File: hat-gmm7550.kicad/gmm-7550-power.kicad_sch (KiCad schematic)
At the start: 47 parts, among them J5 DNI, J6 10144517-064802LF, J8 JTAG, Q1 NX6008NBK, Q2 NX6008NBK, Q3 NX6008NBK, Q4 FDC855N, U2 74LVC1G07, U3 ADM1177, U8 LSF0204PW, U9 LSF0204PW

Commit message: Change U2 footprint due to the part availability, revision and date are updated (HAT GMM-7550)
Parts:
- U2: footprint Package_TO_SOT_SMD:SOT-353_SC-70-5 -> Package_TO_SOT_SMD:SOT-23-5
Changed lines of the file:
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@@
   (title_block
     (title "40-pin GPIO HAT adapter for GMM-7550")
-    (date "2022-03-09")
-    (rev "1.0")
+    (date "2022-04-24")
+    (rev "1.1")
   )
   (junction (at 78.74 172.72) (diameter 0) (color 0 0 0 0)
@@
     (property "Reference" "U2" (id 0) (at 96.52 55.88 0))
     (property "Value" "74LVC1G07" (id 1) (at 100.33 62.23 0))
-    (property "Footprint" "Package_TO_SOT_SMD:SOT-353_SC-70-5" (id 2) (at 93.98 59.69 0)
-      (effects (font (size 1.27 1.27)) hide)
-    )
+    (property "Footprint" "Package_TO_SOT_SMD:SOT-23-5" (id 2) (at 93.98 59.69 0)
+      (effects (font (size 1.27 1.27)) hide)
+    )

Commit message: Update copyright years and increment revision
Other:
- note added: "Copyright (c) 2022-2024 Anton Kuzmin Licensed under CERN-OHL-P v2 https://github.com/gmm-7550/"
- note removed: "Copyright (c) 2022 Anton Kuzmin Licensed under CERN-OHL-P v2 https://github.com/ak-fau/gmm7550.git"
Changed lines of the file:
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@@
   (title_block
     (title "40-pin GPIO HAT adapter for GMM-7550")
-    (date "2022-04-24")
-    (rev "1.1")
+    (date "2024-01-27")
+    (rev "1.2")
   )
   (junction (at 78.74 172.72) (diameter 0) (color 0 0 0 0)
@@
     (effects (font (size 1.27 1.27)) (justify right bottom))
   )
-  (text "Copyright (c) 2022  Anton Kuzmin\nLicensed under CERN-OHL-P v2\nhttps://github.com/ak-fau/gmm7550.git"
+  (text "Copyright (c) 2022-2024  Anton Kuzmin\nLicensed under CERN-OHL-P v2\nhttps://github.com/gmm-7550/"
     (at 198.12 179.07 0)
     (effects (font (size 2.54 2.54)) (justify left bottom))

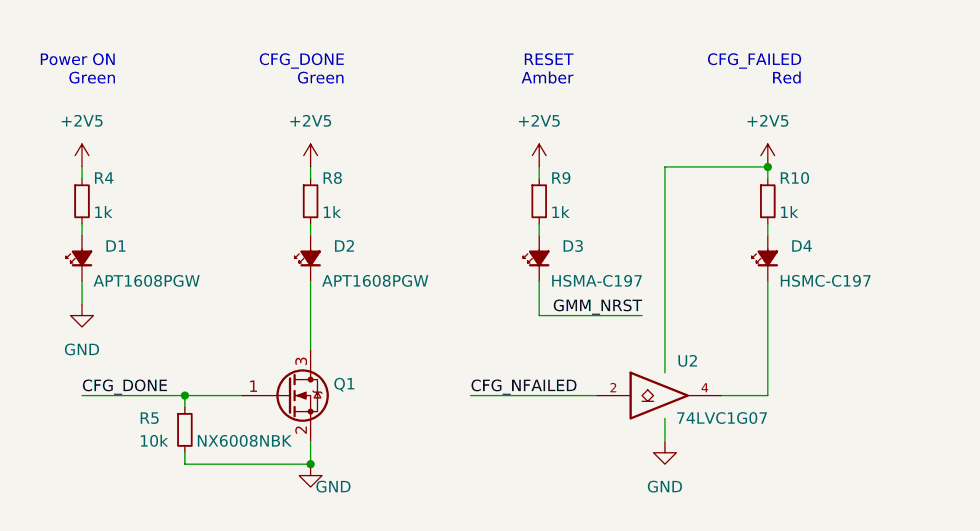
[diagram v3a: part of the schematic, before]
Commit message: Minor updates based on the test results
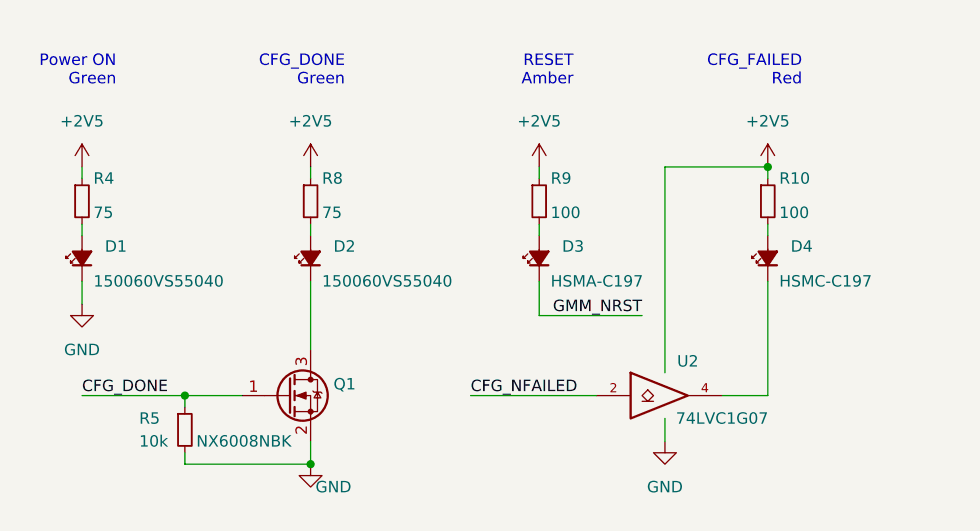
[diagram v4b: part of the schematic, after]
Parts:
- D1, D2: value APT1608PGW -> 150060VS55040
- R10, R9: value 1k -> 100
- R4, R8: value 1k -> 75
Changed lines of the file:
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@@
       (effects (font (size 1.27 1.27)) (justify left))
     )
-    (property "Value" "1k" (at 30.48 39.37 0)
+    (property "Value" "75" (at 30.48 39.37 0)
       (effects (font (size 1.27 1.27)) (justify left))
     )
@@
       (effects (font (size 1.27 1.27)) (justify right))
     )
-    (property "Value" "APT1608PGW" (at 55.88 46.99 90)
+    (property "Value" "150060VS55040" (at 55.88 46.99 90)
       (effects (font (size 1.27 1.27)) (justify right))
     )
@@
       (effects (font (size 1.27 1.27)) (justify left))
     )
-    (property "Value" "1k" (at 81.28 39.37 0)
+    (property "Value" "100" (at 81.28 39.37 0)
       (effects (font (size 1.27 1.27)) (justify left))
     )
@@
       (effects (font (size 1.27 1.27)) (justify left))
     )
-    (property "Value" "1k" (at 106.68 39.37 0)
+    (property "Value" "100" (at 106.68 39.37 0)
       (effects (font (size 1.27 1.27)) (justify left))
     )
@@
       (effects (font (size 1.27 1.27)) (justify left))
     )
-    (property "Value" "1k" (at 55.88 39.37 0)
+    (property "Value" "75" (at 55.88 39.37 0)
       (effects (font (size 1.27 1.27)) (justify left))
     )
@@
       (effects (font (size 1.27 1.27)) (justify right))
     )
-    (property "Value" "APT1608PGW" (at 30.48 46.99 90)
+    (property "Value" "150060VS55040" (at 30.48 46.99 90)
       (effects (font (size 1.27 1.27)) (justify right))
     )

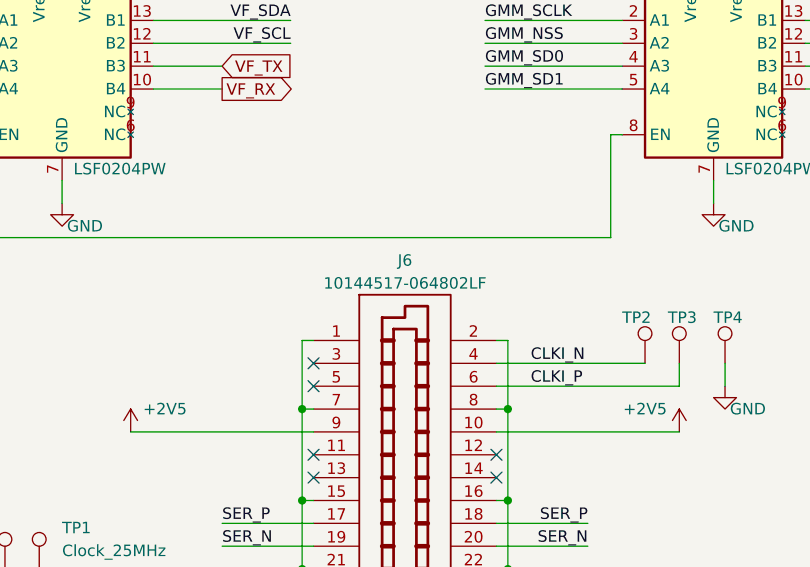
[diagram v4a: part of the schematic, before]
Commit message: Change module connector part number: 9mm board-to-board distance
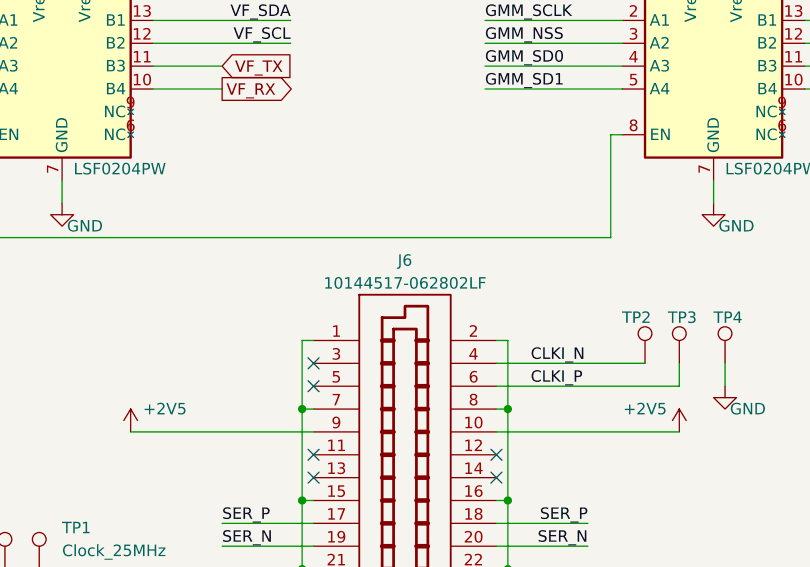
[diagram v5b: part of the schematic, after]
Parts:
- J6: value 10144517-064802LF -> 10144517-062802LF
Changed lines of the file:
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@@
       (effects (font (size 1.27 1.27)))
     )
-    (property "Value" "10144517-064802LF" (at 209.55 66.04 0)
+    (property "Value" "10144517-062802LF" (at 209.55 66.04 0)
       (effects (font (size 1.27 1.27)))
     )
